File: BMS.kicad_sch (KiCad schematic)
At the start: 275 parts, among them CN001 CN001, CN003 S04B-ZESK-2D_T__LF__SN_, CN004 S04B-ZESK-2D_T__LF__SN_, CN2 CN002, IC002 TPS7A1633DGNT, J1 -, J2 Rx, J3 Tx, J4 +, Q001 Q_PNP, Q002 Q_PNP, Q003 Q_PNP, Q004 Q_PNP, Q005 Q_PNP, Q006 ATP304-TL-H, Q007 ATP304-TL-H, Q008 ATP304-TL-H, Q009 ATP304-TL-H, Q010 ATP304-TL-H, Q011 ATP304-TL-H, Q013 Q_PNP, Q014 Q_NPN, Q015 Q_NPN, Q016 Q_NPN, Q017 Q_NPN, Q018 Q_NPN, Q019 Q_NPN, Q020 Q_NPN, Q021 Q_NPN, Q022 Q_NPN, Q023 Q_NPN, Q024 Q_NPN, Q025 Q_NPN, Q026 Q_PMOS, Q027 Q_PMOS, Q028 Q_PMOS, Q12 Q_PNP, U1 BQ77PL900DL

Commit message: Added possible IC003 pinout to README.
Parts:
- removed L1: R22, symbol Device:L_Small
- added R101: 0.22, symbol Device:R_Small
- renumbered JL032 to JL12, JL036 to JL13, JL043 to JL21
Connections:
- net LDO_IN: now also R101.1
- net at Q002.C: now also R101.2
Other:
- note added: "TURNS ON LDO FOR IC003 POWER TRIGGERD VIA RX HIGH OR IC003_PIN19"
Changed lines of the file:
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@@
 	)
 	(rectangle
+		(start 82.55 269.24)
+		(end 184.15 326.39)
+		(stroke
+			(width 0)
+			(type default)
+		)
+		(fill
+			(type none)
+		)
+	)
+	(rectangle
 		(start 368.3 -36.83)
 		(end 420.37 99.06)
@@
 		)
 	)
+	(text "TURNS ON LDO FOR IC003 POWER\nTRIGGERD VIA RX HIGH OR IC003_PIN19"
+		(exclude_from_sim no)
+		(at 83.058 324.358 0)
+		(effects
+			(font
+				(size 1.27 1.27)
+			)
+			(justify left)
+		)
+	)
 	(text "ENABLE DISCHARGE"
 		(exclude_from_sim no)
@@
 		(on_board yes)
 		(dnp no)
-		(property "Reference" "JL043"
+		(property "Reference" "JL21"
 			(at 417.068 150.622 0)
 			(effects
@@
 			(project "BMS"
 				(path "/4e6beee8-2dfa-4c94-aba5-d25855cc9658"
-					(reference "JL043")
+					(reference "JL21")
 					(unit 1)
 				)
@@
 		(on_board yes)
 		(dnp no)
-		(property "Reference" "JL032"
+		(property "Reference" "JL12"
 			(at -74.93 233.68 0)
 			(effects
@@
 			(project "BMS"
 				(path "/4e6beee8-2dfa-4c94-aba5-d25855cc9658"
-					(reference "JL032")
+					(reference "JL12")
 					(unit 1)
 				)
@@
 	)
 	(symbol
-		(lib_id "Device:L_Small")
-		(at 130.81 278.13 90)
-		(unit 1)
-		(exclude_from_sim no)
-		(in_bom yes)
-		(on_board yes)
-		(dnp no)
-		(property "Reference" "L1"
-			(at 130.81 273.812 90)
-			(effects
-				(font
-					(size 1.27 1.27)
-				)
-			)
-		)
-		(property "Value" "R22"
-			(at 130.81 275.59 90)
-			(effects
-				(font
-					(size 1.27 1.27)
-				)
-			)
-		)
-		(property "Footprint" ""
-			(at 130.81 278.13 0)
-			(effects
-				(font
-					(size 1.27 1.27)
-				)
-				(hide yes)
-			)
-		)
-		(property "Datasheet" "~"
-			(at 130.81 278.13 0)
-			(effects
-				(font
-					(size 1.27 1.27)
-				)
-				(hide yes)
-			)
-		)
-		(property "Description" "Inductor, small symbol"
-			(at 130.81 278.13 0)
-			(effects
-				(font
-					(size 1.27 1.27)
-				)
-				(hide yes)
-			)
-		)
-		(pin "2"
-		)
-		(pin "1"
-		)
-		(instances
-			(project ""
-				(path "/4e6beee8-2dfa-4c94-aba5-d25855cc9658"
-					(reference "L1")
-					(unit 1)
-				)
-			)
-		)
-	)
-	(symbol
 		(lib_id "Connector:TestPoint")
 		(at 231.14 20.32 0)
@@
 	)
 	(symbol
+		(lib_id "Device:R_Small")
+		(at 130.81 278.13 90)
+		(mirror x)
+		(unit 1)
+		(exclude_from_sim no)
+		(in_bom yes)
+		(on_board yes)
+		(dnp no)
+		(property "Reference" "R101"
+			(at 129.5399 280.67 0)
+			(effects
+				(font
+					(size 1.016 1.016)
+				)
+				(justify left)
+				(hide yes)
+			)
+		)
+		(property "Value" "0.22"
+			(at 132.842 276.352 90)
+			(effects
+				(font
+					(size 1.27 1.27)
+				)
+				(justify left)
+			)
+		)
+		(property "Footprint" ""
+			(at 130.81 278.13 0)
+			(effects
+				(font
+					(size 1.27 1.27)
+				)
+				(hide yes)
+			)
+		)
+		(property "Datasheet" "~"
+			(at 130.81 278.13 0)
+			(effects
+				(font
+					(size 1.27 1.27)
+				)
+				(hide yes)
+			)
+		)
+		(property "Description" "Resistor, small symbol"
+			(at 130.81 278.13 0)
+			(effects
+				(font
+					(size 1.27 1.27)
+				)
+				(hide yes)
+			)
+		)
+		(pin "2"
+		)
+		(pin "1"
+		)
+		(instances
+			(project "BMS"
+				(path "/4e6beee8-2dfa-4c94-aba5-d25855cc9658"
+					(reference "R101")
+					(unit 1)
+				)
+			)
+		)
+	)
+	(symbol
 		(lib_id "power:GND")
 		(at 92.71 -29.21 90)
@@
 		(on_board yes)
 		(dnp no)
-		(property "Reference" "JL036"
+		(property "Reference" "JL13"
 			(at 135.128 19.812 0)
 			(effects
@@
 			(project "BMS"
 				(path "/4e6beee8-2dfa-4c94-aba5-d25855cc9658"
-					(reference "JL036")
+					(reference "JL13")
 					(unit 1)
 				)

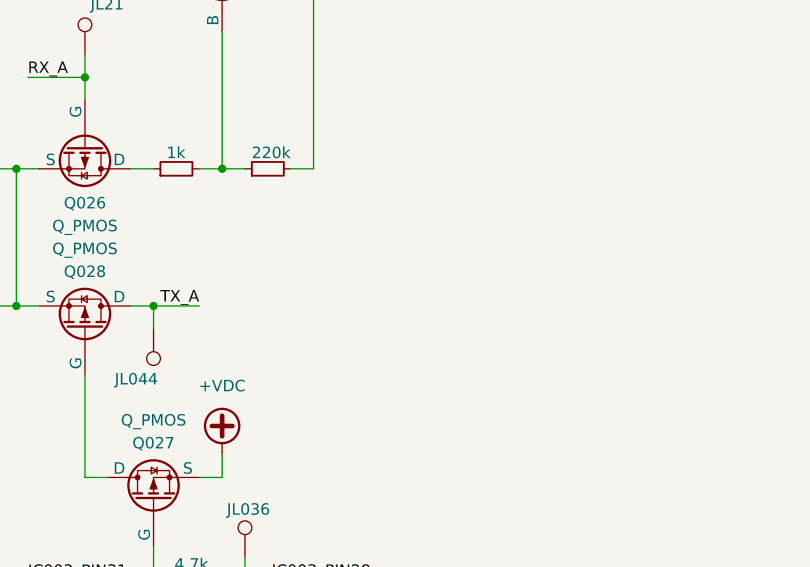
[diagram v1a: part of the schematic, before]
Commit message: Recorded RX/TX between BATT and CHARGER
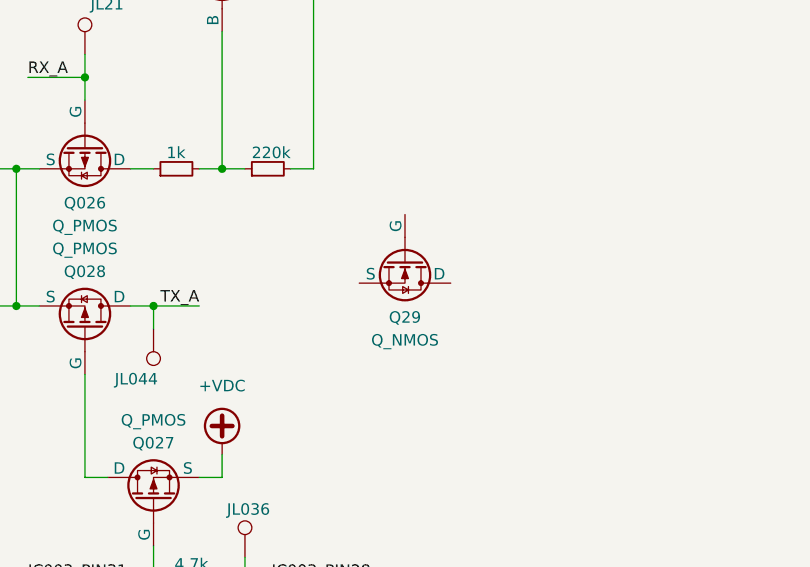
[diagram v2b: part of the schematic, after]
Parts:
- added Q29: Q_NMOS, symbol Device:Q_NMOS
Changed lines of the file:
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@@
+	)
+	(symbol
+		(lib_id "Device:Q_NMOS")
+		(at 448.31 179.07 270)
+		(unit 1)
+		(exclude_from_sim no)
+		(in_bom yes)
+		(on_board yes)
+		(dnp no)
+		(fields_autoplaced yes)
+		(property "Reference" "Q29"
+			(at 448.31 185.42 90)
+			(effects
+				(font
+					(size 1.27 1.27)
+				)
+			)
+		)
+		(property "Value" "Q_NMOS"
+			(at 448.31 187.96 90)
+			(effects
+				(font
+					(size 1.27 1.27)
+				)
+			)
+		)
+		(property "Footprint" ""
+			(at 450.85 184.15 0)
+			(effects
+				(font
+					(size 1.27 1.27)
+				)
+				(hide yes)
+			)
+		)
+		(property "Datasheet" "~"
+			(at 448.31 179.07 0)
+			(effects
+				(font
+					(size 1.27 1.27)
+				)
+				(hide yes)
+			)
+		)
+		(property "Description" "N-MOSFET transistor"
+			(at 448.31 179.07 0)
+			(effects
+				(font
+					(size 1.27 1.27)
+				)
+				(hide yes)
+			)
+		)
+		(pin "G"
+		)
+		(pin "S"
+		)
+		(pin "D"
+		)
+		(instances
+			(project ""
+				(path "/4e6beee8-2dfa-4c94-aba5-d25855cc9658"
+					(reference "Q29")
+					(unit 1)
+				)
+			)
+		)
 	)
 	(symbol

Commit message: Seems I did not push everything, and I updated schematic to show CN001 instead of CN002
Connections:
- net CN002: no longer R59.2, R60.2, R61.2, R62.2, R63.2
- net F_DSG: no longer C36.1, R69.2, R76.1
- net DSG_GATES: now reaches JL016.1, Q006.1 (G), Q007.1 (G), Q008.1 (G), R2.1
- net DSG_GATES: now also C36.1, R69.2, R76.1
- new net CN001: R59.2, R60.2, R61.2, R62.2, R63.2
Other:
- note added: "DISABLE CHARGE"
- note added: "DISABLE DISCHARGE"
- note removed: "ENABLE CHARGE"
- note removed: "ENABLE DISCHARGE"
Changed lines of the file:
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@@
 		)
 	)
-	(text "ENABLE DISCHARGE"
+	(text "DISABLE DISCHARGE"
 		(exclude_from_sim no)
 		(at 431.038 56.134 0)
@@
 		)
 	)
-	(text "ENABLE CHARGE"
+	(text "DISABLE CHARGE"
 		(exclude_from_sim no)
 		(at 429.514 92.964 0)
@@
 	(wire
 		(pts
+			(xy -125.73 16.51) (xy -140.97 16.51)
+		)
+		(stroke
+			(width 0)
+			(type default)
+		)
+	)
+	(wire
+		(pts
 			(xy 148.59 229.87) (xy 148.59 232.41)
 		)
@@
 		)
 	)
-	(label "CN002"
+	(label "CN001"
 		(at 303.53 -21.59 0)
 		(effects
@@
 		)
 	)
-	(label "CN002"
+	(label "CN001"
 		(at 303.53 39.37 0)
 		(effects
@@
 		)
 	)
-	(label "CN002"
+	(label "CN001"
 		(at 303.53 -1.27 0)
 		(effects
@@
 		)
 	)
-	(label "CN002"
+	(label "CN001"
 		(at 303.53 19.05 0)
 		(effects
@@
 		)
 	)
-	(label "CN002"
+	(label "DSG_GATES"
+		(at -140.97 16.51 0)
+		(effects
+			(font
+				(size 1.27 1.27)
+			)
+			(justify left bottom)
+		)
+	)
+	(label "CN001"
 		(at 303.53 59.69 0)
 		(effects
@@
 		)
 	)
-	(label "F_DSG"
-		(at 455.93 88.9 0)
-		(effects
-			(font
-				(size 1.27 1.27)
-			)
-			(justify left bottom)
-		)
-	)
 	(label "PACK_P"
 		(at 170.18 255.27 180)
@@
 		)
 	)
+	(label "DSG_GATES"
+		(at 455.93 88.9 0)
+		(effects
+			(font
+				(size 1.27 1.27)
+			)
+			(justify left bottom)
+		)
+	)
